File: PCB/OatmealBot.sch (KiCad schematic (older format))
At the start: 27 parts, among them J1 TerminalBlock_5pin_3.5mm, J10 ServoHeader3, J2 RPi_GPIO, J3 TerminalBlock_5pin_3.5mm, J4 ServoHeader1, J5 Motor 3, J6 Motor 4, J7 ServoHeader2, J8 Motor 1, J9 Motor 2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

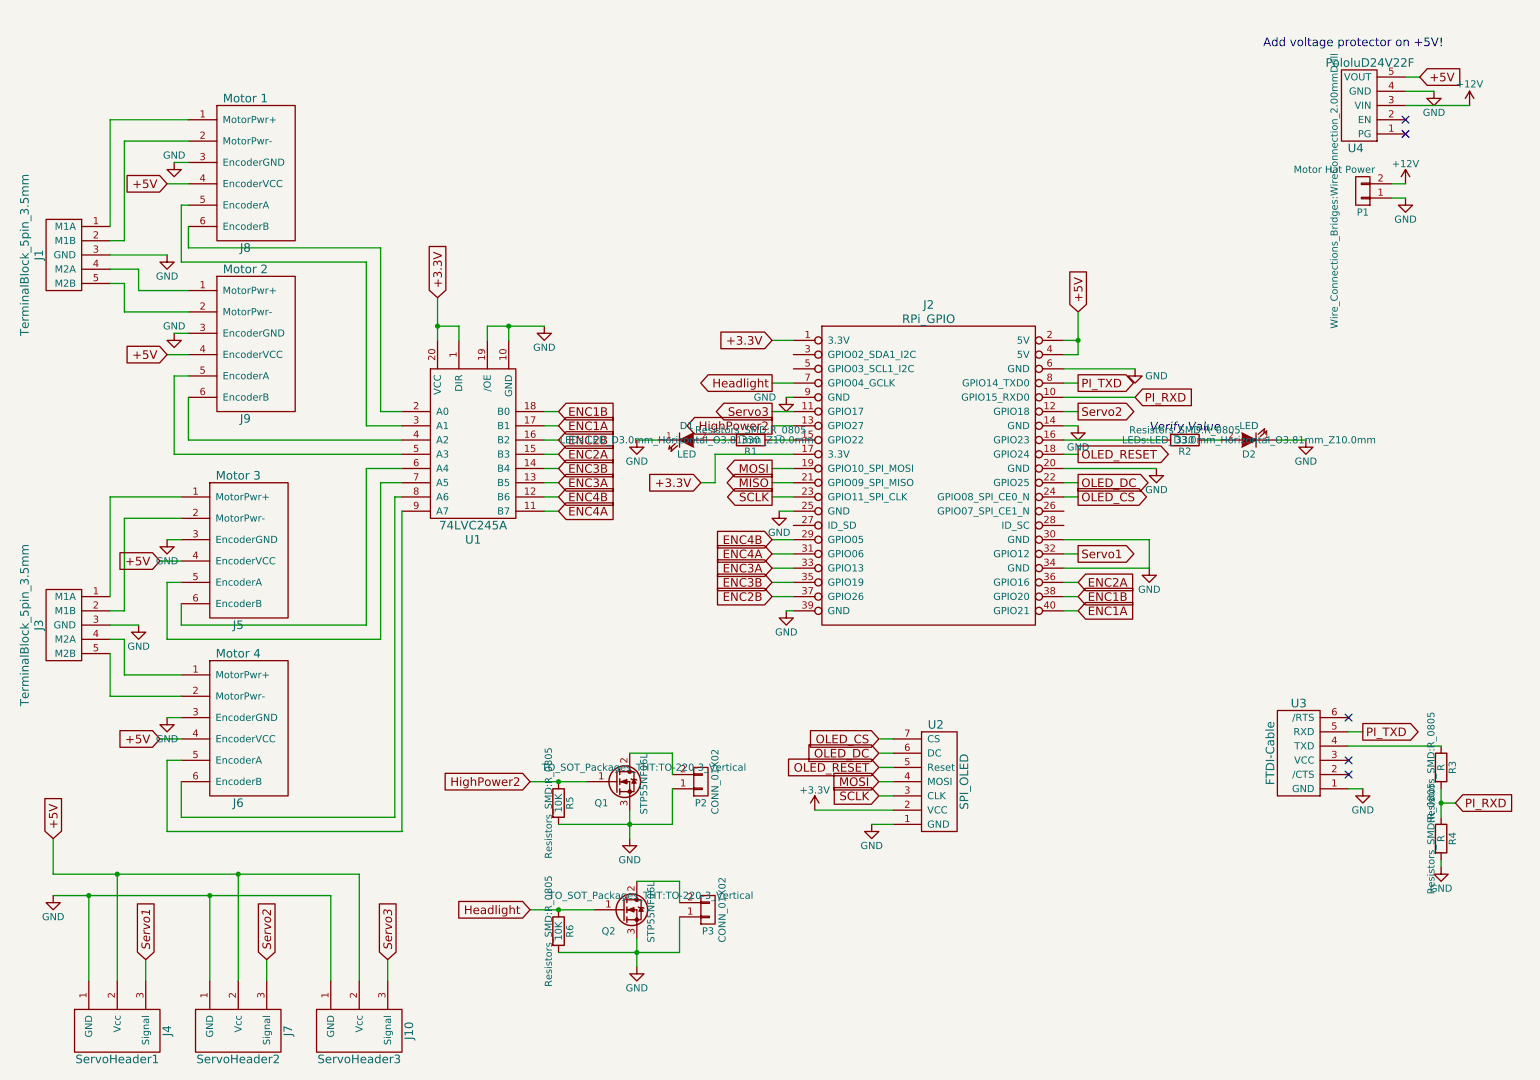
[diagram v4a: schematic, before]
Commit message: Added 4 more servo headers for the extra PWM outputs. Rearranged the schematic a little to fix in US letter size paper.
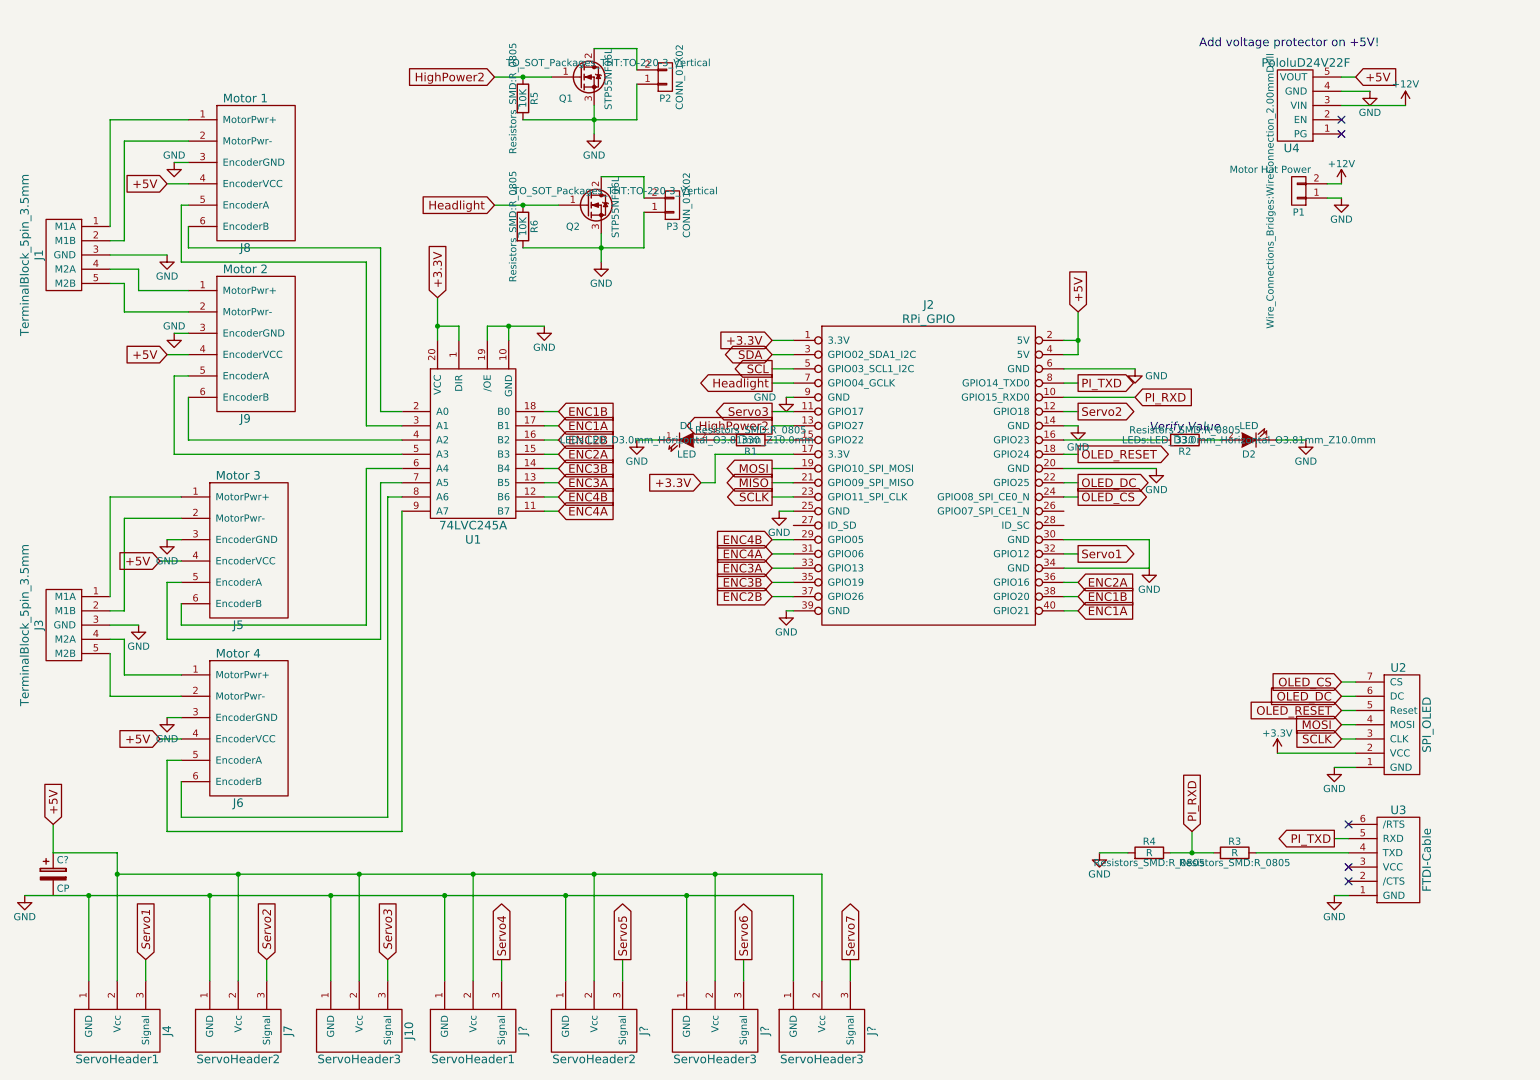
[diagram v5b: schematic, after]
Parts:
- added C?: CP, symbol CP
- added J?: ServoHeader1, Pin_Headers:Pin_Header_Straight_1x03_Pitch2.54mm, symbol ServoHeader
- added J?: ServoHeader2, Pin_Headers:Pin_Header_Straight_1x03_Pitch2.54mm, symbol ServoHeader
- added J? (x2): ServoHeader3, Pin_Headers:Pin_Header_Straight_1x03_Pitch2.54mm, symbol ServoHeader
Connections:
- net +5V: now also C?.1, J?.2 (Vcc), J?.2 (Vcc), J?.2 (Vcc), J?.2 (Vcc)
- net GND: now also J?.1 (GND), J?.1 (GND), J?.1 (GND), J?.1 (GND)
- net SDA: now reaches J2.3 (GPIO02_SDA1_I2C)
- net SCL: now reaches J2.5 (GPIO03_SCL1_I2C)
- new net Servo4: J?.3 (Signal)
- new net Servo5: J?.3 (Signal)
- new net Servo6: J?.3 (Signal)
- new net Servo7: J?.3 (Signal)
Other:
- moved on the sheet: P1, P2, P3, Q1, Q2, R3, R4, R5, R6, U2, U3, U4
